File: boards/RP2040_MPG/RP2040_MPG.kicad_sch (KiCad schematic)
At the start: 5 parts, among them J1 RJ12, SW1 SW_Push, U2 RS485_2_TTL_UART

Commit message: WIP
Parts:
- added H1, H2, H3, H4: MountingHole, MountingHole:MountingHole_3.2mm_M3_DIN965, symbol Mechanical:MountingHole
- added J2: Conn_01x04_Socket, Connector_Molex:Molex_KK-254_AE-6410-04A_1x04_P2.54mm_Vertical, symbol Connector:Conn_01x04_Socket
- added SW2, SW3, SW4: SW_Push, Heli2:Drucktaster_12x12, symbol Switch:SW_Push
- J1: footprint (none) -> Connector_RJ:RJ12_Amphenol_54601
- SW1: footprint (none) -> Heli2:Drucktaster_12x12
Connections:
- net GND: now also Brd1.2 (GND), J1.6, U2.7 (Y), J2.2 (Pin_2), SW2.2, SW3.2, SW4.2; no longer Brd1.1 (GND)
- net at RZ1.21 (3V3), U2.1 (VCC): now also Brd1.1 (VCC), J2.1 (Pin_1); no longer Brd1.2 (VCC)
- net at J1.1: now also RZ1.22 (5V)
- net at RZ1.11 (GP10): now also J2.4 (Pin_4)
- net at RZ1.12 (GP11): now also J2.3 (Pin_3)
- net at RZ1.14 (GP13): now also SW4.1
- net at RZ1.15 (GP14): now also SW3.1
- net at RZ1.16 (GP15): now also SW2.1
- no-connect marks 0 -> 1

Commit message: add title
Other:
- note added: "MPG wheel with RS485 and a OLED-display SSD1306. (c) Heli², Christian Jung"
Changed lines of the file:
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@@
     (stroke (width 0) (type default))
+  )
+  (text "MPG wheel with RS485 and a OLED-display SSD1306.\n\n(c) Heli², Christian Jung"
+    (at 191.77 175.26 0)
+    (effects (font (size 1.27 1.27)) (justify left bottom))
   )
   (symbol (lib_id "oled_lcd_tft_displays:SSD1306") (at 83.82 71.12 270) (mirror x) (unit 1)

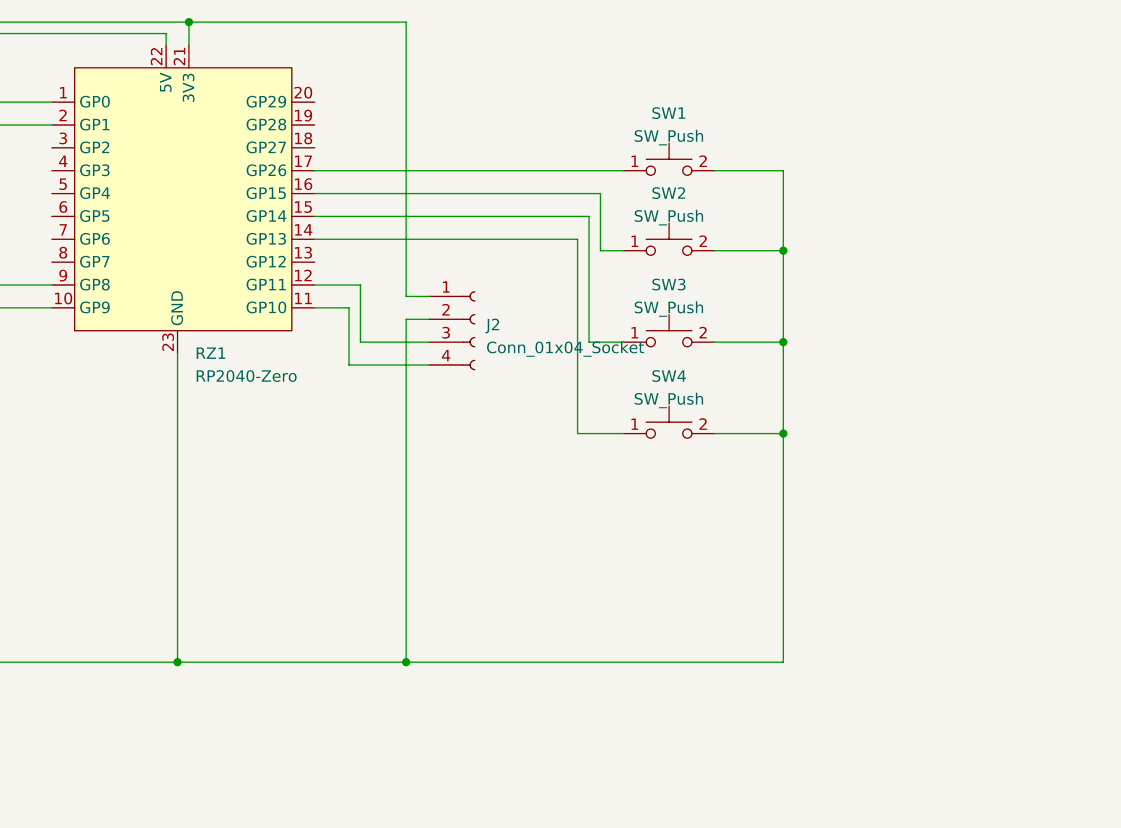
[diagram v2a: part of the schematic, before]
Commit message: add RC vor switches and MPG
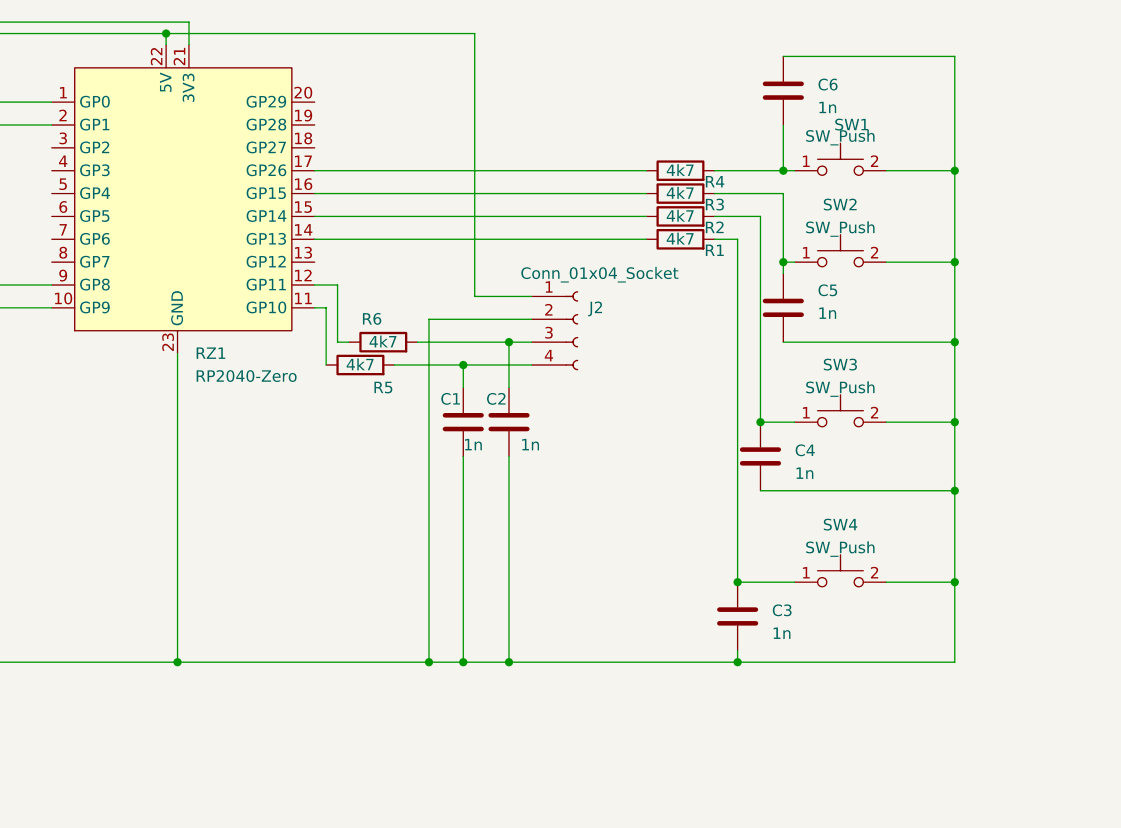
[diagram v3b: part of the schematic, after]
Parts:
- added C1, C2, C3, C4, C5, C6: 1n, symbol Device:C
- added R1, R2, R3, R4, R5, R6: 4k7, Resistor_THT:R_Axial_DIN0204_L3.6mm_D1.6mm_P5.08mm_Horizontal, symbol Device:R
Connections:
- net GND: now also C1.2, C2.2, C3.2, C4.2, C5.2, C6.1
- net at Brd1.1 (VCC), RZ1.21 (3V3), U2.1 (VCC): no longer J2.1 (Pin_1)
- net at SW1.1: now also C6.2, R4.2; no longer RZ1.17 (GP26)
- net at SW2.1: now also C5.1, R3.2; no longer RZ1.16 (GP15)
- net at SW3.1: now also C4.1, R2.2; no longer RZ1.15 (GP14)
- net at SW4.1: now also C3.1, R1.2; no longer RZ1.14 (GP13)
- net at J2.3 (Pin_3): now also C2.1, R6.2; no longer RZ1.12 (GP11)
- net at RZ1.11 (GP10): now also R5.1; no longer J2.4 (Pin_4)
- net at J1.1, RZ1.22 (5V): now also J2.1 (Pin_1)
- new net: C1.1, J2.4 (Pin_4), R5.2
- new net: R6.1, RZ1.12 (GP11)
- new net: R3.1, RZ1.16 (GP15)
- new net: R4.1, RZ1.17 (GP26)
- new net: R2.1, RZ1.15 (GP14)
- new net: R1.1, RZ1.14 (GP13)
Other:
- moved on the sheet: J2, SW1, SW2, SW3, SW4

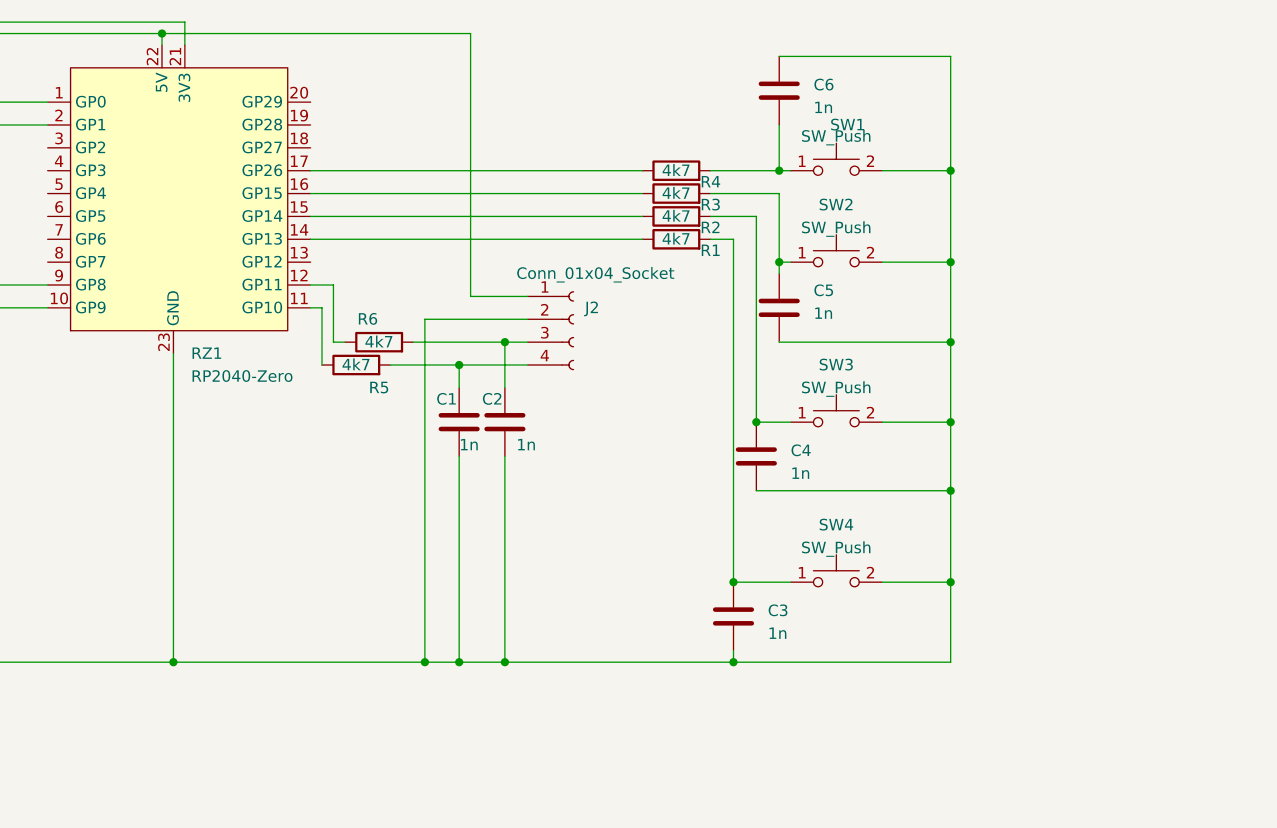
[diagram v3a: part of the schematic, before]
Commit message: change rc filter
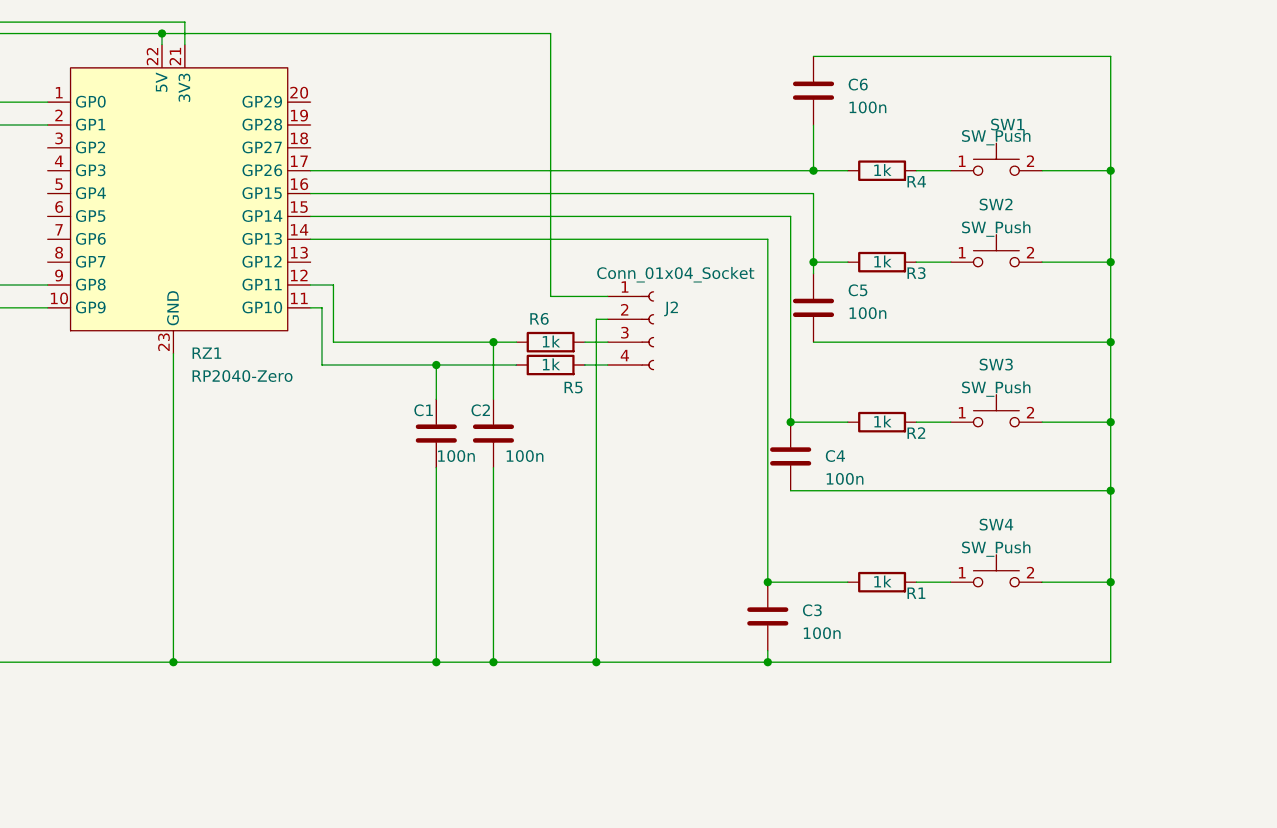
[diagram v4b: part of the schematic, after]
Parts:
- C1, C2, C3, C4, C5, C6: value 1n -> 100n
- R1, R2, R3, R4, R5, R6: value 4k7 -> 1k
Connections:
- net at J2.3 (Pin_3), R6.2: no longer C2.1
- net at R5.1, RZ1.11 (GP10): now also C1.1
- net at J2.4 (Pin_4), R5.2: no longer C1.1
- net at R4.2, SW1.1: no longer C6.2
- net at R3.2, SW2.1: no longer C5.1
- net at R6.1, RZ1.12 (GP11): now also C2.1
- net at R3.1, RZ1.16 (GP15): now also C5.1
- net at R4.1, RZ1.17 (GP26): now also C6.2
- net at R2.2, SW3.1: no longer C4.1
- net at R1.2, SW4.1: no longer C3.1
- net at R2.1, RZ1.15 (GP14): now also C4.1
- net at R1.1, RZ1.14 (GP13): now also C3.1
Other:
- moved on the sheet: C1, C2, C3, C4, C5, C6, J2, R4, SW1, SW2, SW3, SW4

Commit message: add 4xswitches
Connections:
- net GND: no longer U2.7 (Y)
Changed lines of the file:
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@@
   (junction (at 157.48 73.66) (diameter 0) (color 0 0 0 0)
-  )
-  (junction (at 62.23 54.61) (diameter 0) (color 0 0 0 0)
   )
   (junction (at 168.91 109.22) (diameter 0) (color 0 0 0 0)
@@
     (stroke (width 0) (type default))
   )
-  (wire (pts (xy 62.23 54.61) (xy 76.2 54.61))
-    (stroke (width 0) (type default))
-  )
   (wire (pts (xy 87.63 49.53) (xy 107.95 49.53))
     (stroke (width 0) (type default))
@@
     (stroke (width 0) (type default))
   )
-  (wire (pts (xy 62.23 54.61) (xy 62.23 50.8))
-    (stroke (width 0) (type default))
-  )
   (wire (pts (xy 120.65 39.37) (xy 120.65 40.64))
     (stroke (width 0) (type default))
@@
     (stroke (width 0) (type default))
   )
-  (wire (pts (xy 55.88 54.61) (xy 62.23 54.61))
-    (stroke (width 0) (type default))
-  )
+  (wire (pts (xy 55.88 54.61) (xy 76.2 54.61))
+    (stroke (width 0) (type default))
+  )
